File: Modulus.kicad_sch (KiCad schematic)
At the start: 224 parts, among them J1 XLR3, J2 USB_C_Receptacle_USB2.0_14P, J3 USB_A, J4 USB_A, J5 XLR3, J6 OLED_128x32, SW1 Push_Button, U1 RP2040, U2 NCP1117-1.5_SOT223, U3 W25Q128JVS, U4 MT3608, Y1 12MHz

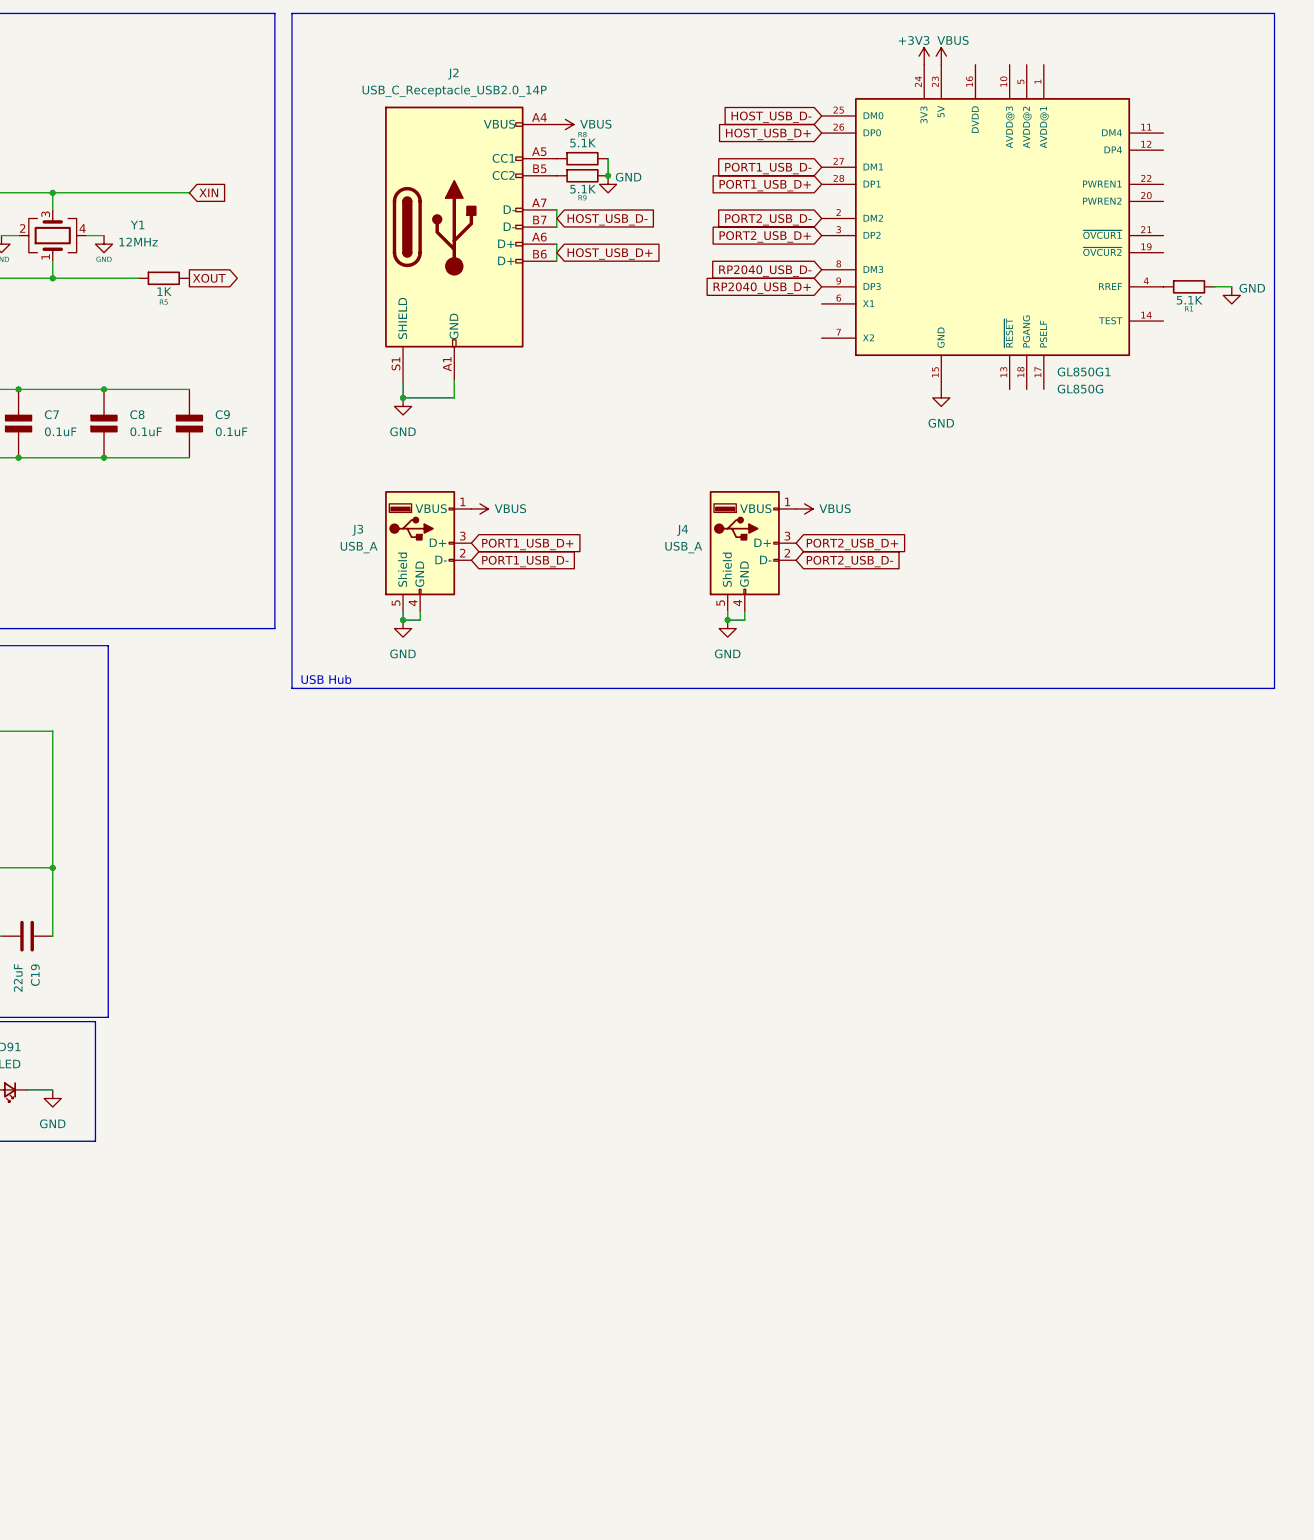
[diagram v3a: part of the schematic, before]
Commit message: Finished the schematic design for this! creating modular boardas another project
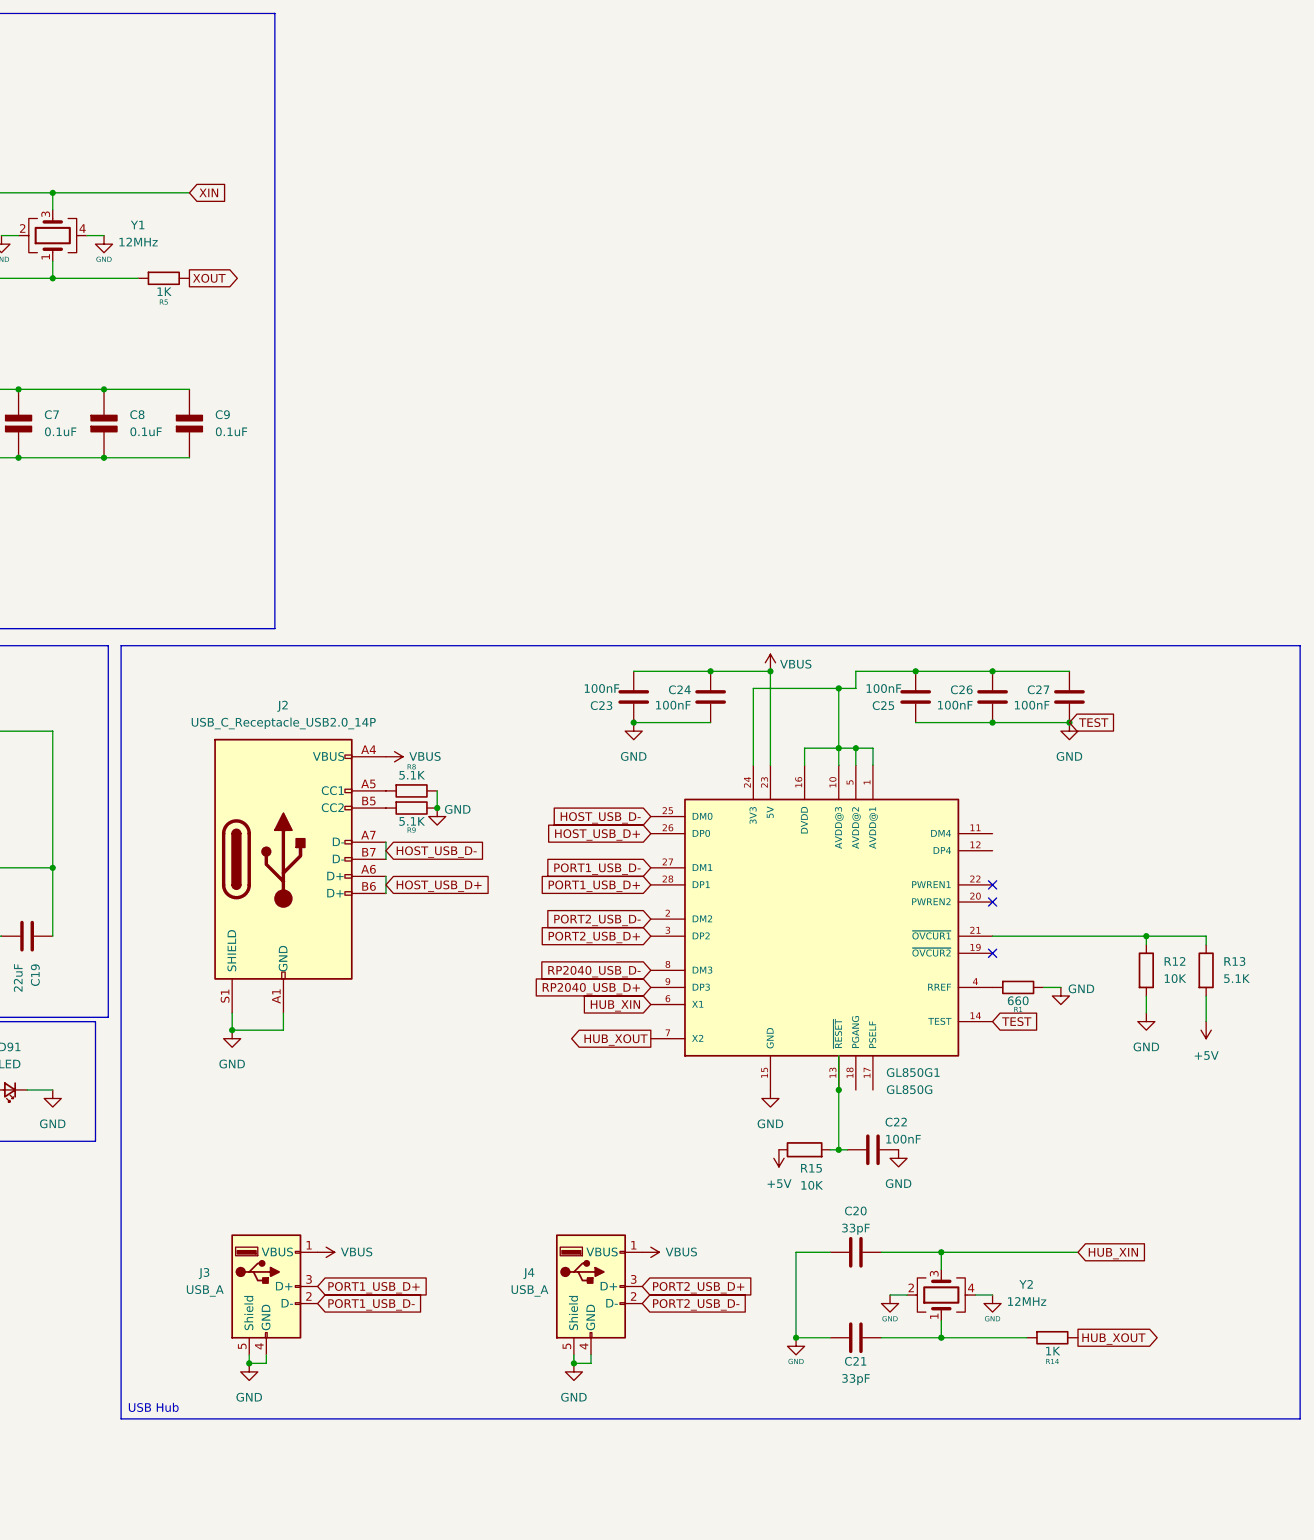
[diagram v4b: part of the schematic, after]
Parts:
- added C20, C21: 33pF, symbol Device:C
- added C22: 100nF, Capacitor_SMD:C_0603_1608Metric_Pad1.08x0.95mm_HandSolder, symbol Device:C
- added C23, C24, C25, C26, C27: 100nF, symbol Device:C
- added R12, R15: 10K, Resistor_SMD:R_0603_1608Metric_Pad0.98x0.95mm_HandSolder, symbol Device:R
- added R13: 5.1K, Resistor_SMD:R_0603_1608Metric_Pad0.98x0.95mm_HandSolder, symbol Device:R
- added R14: 1K, Resistor_THT:R_Axial_DIN0207_L6.3mm_D2.5mm_P10.16mm_Horizontal, symbol PCM_SL_Resistors:Resistor
- added Y2: 12MHz, symbol Device:Crystal_GND24
- R1: value 5.1K -> 660
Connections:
- net +3V3: no longer GL850G1.24 (3V3)
- net GND: now also GL850G1.14 (TEST), C20.1, C21.1, C22.1, C23.1, C24.1, C25.1, C26.1, C27.1, R12.2, Y2.2, Y2.4
- net VBUS: now also C23.2, C24.2
- net at GL850G1.1 (AVDD@1): now also GL850G1.10 (AVDD@3), GL850G1.16 (DVDD), GL850G1.24 (3V3), GL850G1.5 (AVDD@2), C25.2, C26.2, C27.2
- net at GL850G1.13 (~{RESET}): now also C22.2, R15.2
- net at GL850G1.21 (~{OVCUR1}): now also R12.1, R13.1
- net HUB_XIN: now reaches GL850G1.6 (X1)
- net HUB_XIN: now also C20.2, Y2.3
- net HUB_XOUT: now reaches GL850G1.7 (X2)
- net HUB_XOUT: now also R14.2
- new net: C21.2, R14.1, Y2.1
- new net +5V: R13.2, R15.1
- no-connect marks 0 -> 3
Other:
- moved on the sheet: GL850G1, J2, J3, J4, R1, R8, R9

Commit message: ts so difficult :sob: - anyways completed wiring first row, and the MCUs
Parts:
- removed C18: 10uF, symbol Device:C
- removed C19: 22uF, symbol Device:C
- removed D90: SS34, PCM_Diode_SMD_AKL:D_SMC, symbol PCM_Diode_Schottky_AKL:SS34
- removed J2: USB_C_Receptacle_USB2.0_14P, symbol Connector:USB_C_Receptacle_USB2.0_14P
- removed L1: 4.7uH, symbol PCM_Elektuur:L
- removed U4: MT3608, Package_TO_SOT_SMD:SOT-23-6, symbol Regulator_Switching:MT3608
- added J2: USB_C_Receptacle_USB2.0_16P, ScottoKeebs_Components:USB_C_HRO_TYPE-C-31-M-12, symbol Connector:USB_C_Receptacle_USB2.0_16P
- added R16, R17: 10k, PCM_Resistor_SMD_AKL:R_1206_3216Metric, symbol PCM_SL_Resistors:Resistor
- -_1: renamed from S26; footprint (none) -> ScottoKeebs_Hotswap:Hotswap_MX_1.00u
- -_D1: renamed from D26; footprint (none) -> Diode_SMD:D_SMA
- 0)1: renamed from S25; footprint (none) -> ScottoKeebs_Hotswap:Hotswap_MX_1.00u
- 0)D1: renamed from D25; footprint (none) -> Diode_SMD:D_SMA
- 1!1: renamed from S16; footprint (none) -> ScottoKeebs_Hotswap:Hotswap_MX_1.00u
- 1!D1: renamed from D16; footprint (none) -> Diode_SMD:D_SMA
- 2@1: renamed from S17; footprint (none) -> ScottoKeebs_Hotswap:Hotswap_MX_1.00u
- 2@D1: renamed from D17; footprint (none) -> Diode_SMD:D_SMA
- 3#1: renamed from S18; footprint (none) -> ScottoKeebs_Hotswap:Hotswap_MX_1.00u
- 3#D1: renamed from D18; footprint (none) -> Diode_SMD:D_SMA
- 4$1: renamed from S19; footprint (none) -> ScottoKeebs_Hotswap:Hotswap_MX_1.00u
- 4$D1: renamed from D19; footprint (none) -> Diode_SMD:D_SMA
- 5%1: renamed from S20; footprint (none) -> ScottoKeebs_Hotswap:Hotswap_MX_1.00u
- 5%D1: renamed from D20; footprint (none) -> Diode_SMD:D_SMA
- 6^1: renamed from S21; footprint (none) -> ScottoKeebs_Hotswap:Hotswap_MX_1.00u
- 6^D1: renamed from D21; footprint (none) -> Diode_SMD:D_SMA
- 7&1: renamed from S22; footprint (none) -> ScottoKeebs_Hotswap:Hotswap_MX_1.00u
- 7&D1: renamed from D22; footprint (none) -> Diode_SMD:D_SMA
- 8*1: renamed from S23; footprint (none) -> ScottoKeebs_Hotswap:Hotswap_MX_1.00u
- 8*D1: renamed from D23; footprint (none) -> Diode_SMD:D_SMA
- 9(1: renamed from S24; footprint (none) -> ScottoKeebs_Hotswap:Hotswap_MX_1.00u
- 9(D1: renamed from D24; footprint (none) -> Diode_SMD:D_SMA
- =+1: renamed from S27; footprint (none) -> ScottoKeebs_Hotswap:Hotswap_MX_1.00u
- =+D1: renamed from D27; footprint (none) -> Diode_SMD:D_SMA
- Backspace1: renamed from S28; footprint (none) -> ScottoKeebs_Hotswap:Hotswap_MX_1.00u
- Backspace2: renamed from S29; footprint (none) -> ScottoKeebs_Hotswap:Hotswap_MX_1.00u
- BackspaceD1: renamed from D28; footprint (none) -> Diode_SMD:D_SMA
- BackspaceD2: renamed from D29; footprint (none) -> Diode_SMD:D_SMA
- C1, C10, C11, C12, C17, C2, C23, C24, C25, C26, C27, C3, C4, C5, C6, C7, C8, C9: footprint (none) -> Capacitor_SMD:C_0402_1005Metric
- C13, C14, C15, C16, C20, C21: footprint (none) -> Capacitor_SMD:C_0201_0603Metric
- C22: footprint Capacitor_SMD:C_0603_1608Metric_Pad1.08x0.95mm_HandSolder -> Capacitor_SMD:C_0402_1005Metric
- Command1, Command2, Control1, Control2, Down1, Fn1, Left1, Option1, Option2, PgDown1, PgUp1, Right1, S32, S33, S34, S35, S36, S37, S38, S39, S40, S41, S42, S43, S46, S47, S48, S49, S50, S51, S52, S53, S54, S55, S56, S57, S61, S62, S63, S64, S65, S66, S67, S68, S69, S70, S71: footprint (none) -> ScottoKeebs_Hotswap:Hotswap_MX_1.00u
- D31, D32, D33, D34, D35, D36, D37, D38, D39, D40, D41, D42, D43, D44, D45, D46, D47, D48, D49, D50, D51, D52, D53, D54, D55, D56, D57, D58, D59, D60, D61, D62, D63, D64, D65, D66, D67, D68, D69, D70, D71, D72, D73, D74, D75, D76, D77, D78, D79, D80, D81, D82, D83, D84, D85, D86, D87, D88, D89: footprint (none) -> Diode_SMD:D_SMA
- D91: footprint SparkFun-LED:LED_0603_1608Metric -> Green_LED:0603
- Del1: renamed from S14; footprint (none) -> ScottoKeebs_Hotswap:Hotswap_MX_1.00u
- Del2: renamed from S30; footprint (none) -> ScottoKeebs_Hotswap:Hotswap_MX_1.00u
- DelD1: renamed from D14; footprint (none) -> Diode_SMD:D_SMA
- DelD2: renamed from D30; footprint (none) -> Diode_SMD:D_SMA
- Esc1: renamed from S1; footprint (none) -> ScottoKeebs_Hotswap:Hotswap_MX_1.00u
- EscD1: renamed from D1; footprint (none) -> Diode_SMD:D_SMA
- F1: renamed from S2; footprint (none) -> ScottoKeebs_Hotswap:Hotswap_MX_1.00u
- F10: renamed from S11; footprint (none) -> ScottoKeebs_Hotswap:Hotswap_MX_1.00u
- F10D1: renamed from D11; footprint (none) -> Diode_SMD:D_SMA
- F11: renamed from S12; footprint (none) -> ScottoKeebs_Hotswap:Hotswap_MX_1.00u
- F11D1: renamed from D12; footprint (none) -> Diode_SMD:D_SMA
- F12: renamed from S13; footprint (none) -> ScottoKeebs_Hotswap:Hotswap_MX_1.00u
- F12D1: renamed from D13; footprint (none) -> Diode_SMD:D_SMA
- F1D1: renamed from D2; footprint (none) -> Diode_SMD:D_SMA
- F2: renamed from S3; footprint (none) -> ScottoKeebs_Hotswap:Hotswap_MX_1.00u
- F2D1: renamed from D3; footprint (none) -> Diode_SMD:D_SMA
- F3: renamed from S4; footprint (none) -> ScottoKeebs_Hotswap:Hotswap_MX_1.00u
- F3D1: renamed from D4; footprint (none) -> Diode_SMD:D_SMA
- F4: renamed from S5; footprint (none) -> ScottoKeebs_Hotswap:Hotswap_MX_1.00u
- F4D1: renamed from D5; footprint (none) -> Diode_SMD:D_SMA
- F5: renamed from S6; footprint (none) -> ScottoKeebs_Hotswap:Hotswap_MX_1.00u
- F5D1: renamed from D6; footprint (none) -> Diode_SMD:D_SMA
- F6: renamed from S7; footprint (none) -> ScottoKeebs_Hotswap:Hotswap_MX_1.00u
- F6D1: renamed from D7; footprint (none) -> Diode_SMD:D_SMA
- F7: renamed from S8; footprint (none) -> ScottoKeebs_Hotswap:Hotswap_MX_1.00u
- F7D1: renamed from D8; footprint (none) -> Diode_SMD:D_SMA
- F8: renamed from S9; footprint (none) -> ScottoKeebs_Hotswap:Hotswap_MX_1.00u
- F8D1: renamed from D9; footprint (none) -> Diode_SMD:D_SMA
- F9: renamed from S10; footprint (none) -> ScottoKeebs_Hotswap:Hotswap_MX_1.00u
- F9D1: renamed from D10; footprint (none) -> Diode_SMD:D_SMA
- J1, J5: footprint (none) -> NC3FAAH:NEUTRIK_NC3FAAH
- J3, J4: footprint (none) -> USB1046-GF-0190-L-B-A_REVB4:GCT_USB1046-GF-0190-L-B-A_REVB4
- R1: value 660 -> 220; footprint Resistor_THT:R_Axial_DIN0207_L6.3mm_D2.5mm_P10.16mm_Horizontal -> PCM_Resistor_SMD_AKL:R_0201_0603Metric
- R10, R2: value 88.7K -> 220; footprint Resistor_THT:R_Axial_DIN0207_L6.3mm_D2.5mm_P10.16mm_Horizontal -> PCM_Resistor_SMD_AKL:R_0201_0603Metric
- R11, R3, R4, R8, R9: footprint Resistor_THT:R_Axial_DIN0207_L6.3mm_D2.5mm_P10.16mm_Horizontal -> PCM_Resistor_SMD_AKL:R_0402_1005Metric
- R12, R15: footprint Resistor_SMD:R_0603_1608Metric_Pad0.98x0.95mm_HandSolder -> PCM_Resistor_SMD_AKL:R_1206_3216Metric
- R13: footprint Resistor_SMD:R_0603_1608Metric_Pad0.98x0.95mm_HandSolder -> PCM_Resistor_SMD_AKL:R_0402_1005Metric
- R14, R5, R6: footprint Resistor_THT:R_Axial_DIN0207_L6.3mm_D2.5mm_P10.16mm_Horizontal -> Resistor_SMD:R_1206_3216Metric
- R7: footprint Resistor_THT:R_Axial_DIN0207_L6.3mm_D2.5mm_P10.16mm_Horizontal -> PCM_Resistor_SMD_AKL:R_1206_3216Metric
- S31, S44, S60, Space1, Space2, Space3, Space4: footprint (none) -> ScottoKeebs_Hotswap:Hotswap_MX_1.50u
- S45: footprint (none) -> ScottoKeebs_Hotswap:Hotswap_MX_1.75u
- S58, S59, S72: footprint (none) -> ScottoKeebs_Hotswap:Hotswap_MX_1.25u
- UP1: footprint (none) -> ScottoKeebs_MX:MX_PCB_1.00u
- Y1, Y2: footprint (none) -> Crystal:Crystal_SMD_3225-4Pin_3.2x2.5mm
- `~1: renamed from S15; footprint (none) -> ScottoKeebs_Hotswap:Hotswap_MX_1.00u
- `~D1: renamed from D15; footprint (none) -> Diode_SMD:D_SMA
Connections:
- net USB_D+ is gone; now on net RP2040_USB_D+: R3.1
- net USB_D- is gone; now on net RP2040_USB_D-: R4.1
- net +3V3: now also C25.2, C26.2, C27.2, GL850G1.1 (AVDD@1), GL850G1.10 (AVDD@3), GL850G1.16 (DVDD), GL850G1.24 (3V3), GL850G1.5 (AVDD@2)
- net CAPS_LOCK_LED: no longer U1.41 (GPIO29_ADC3)
- net GND: now also R10.1, J2.A1 (GND), J2.A12 (GND), J2.B1 (GND), J2.B12 (GND), J2.S1 (SHIELD); no longer R1.2, R10.2, R2.2
- net HOST_USB_D+: now also J2.A6 (D+), J2.B6 (D+)
- net HOST_USB_D-: now also J2.A7 (D-), J2.B7 (D-)
- net OLED_SCL: now also R17.1; no longer J6.3 (SCL)
- net OLED_SDA: now also R16.1; no longer J6.4 (SDA)
- net VBUS: now also J5.2, J2.A4 (VBUS), J2.A9 (VBUS), J2.B4 (VBUS), J2.B9 (VBUS)
- net at R8.1: now also J2.A5 (CC1)
- net at R2.1: now also R1.2; no longer R10.1
- net at R9.1: now also J2.B5 (CC2)
- new net: R10.2, R2.2
- new net: J6.3 (SCL), R17.2
- new net: J6.4 (SDA), R16.2
- no-connect marks 3 -> 9
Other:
- note removed: "Transmits 12V instead of 5v or 3v3"
- moved on the sheet: J6

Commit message: wired everything, but didn't run DRC-
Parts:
- removed Control2: Keyswitch, ScottoKeebs_Hotswap:Hotswap_MX_1.00u, symbol SCOTOKEEBS:Placeholder_Keyswitch
- removed D83: Diode, Diode_SMD:D_SMA, symbol SCOTOKEEBS:Placeholder_Diode
- S60: footprint ScottoKeebs_Hotswap:Hotswap_MX_1.50u -> ScottoKeebs_Hotswap:Hotswap_MX_1.25u
- S72: footprint ScottoKeebs_Hotswap:Hotswap_MX_1.25u -> ScottoKeebs_Hotswap:Hotswap_MX_1.50u
- UP1: footprint ScottoKeebs_MX:MX_PCB_1.00u -> ScottoKeebs_Hotswap:Hotswap_MX_1.00u
- renumbered S34 to E1, S39 to I1, S40 to O1, S41 to P1, S32 to Q1, S35 to RKey1, S36 to T1, S31 to Tab1, S38 to UKey1, S33 to W1, S37 to YKey11, S42 to [{1, S44 to \|1, S43 to ]}1
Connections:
- net COL_10: now also Left1.1, PgUp1.1
- net COL_11: now also Down1.1, UP1.1; no longer Left1.1, PgUp1.1
- net COL_12: now also PgDown1.1, Right1.1; no longer Down1.1, UP1.1
- net COL_13: no longer PgDown1.1, Right1.1
- net PORT2_USB_D+: now also GL850G1.12 (DP4); no longer GL850G1.3 (DP2)
- net PORT2_USB_D-: now also GL850G1.11 (DM4); no longer GL850G1.2 (DM2)
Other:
- moved on the sheet: D84, D85, D86, D87, D88, D89, Down1, Left1, PgDown1, PgUp1, Right1, UP1
